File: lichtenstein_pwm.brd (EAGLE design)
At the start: 73.9 x 54.2 mm, 58 parts, among them IC1 LM2852Y-3V3, IC2 MCP23017, J1 MAGJACK, U1 ONION-OMEGA2

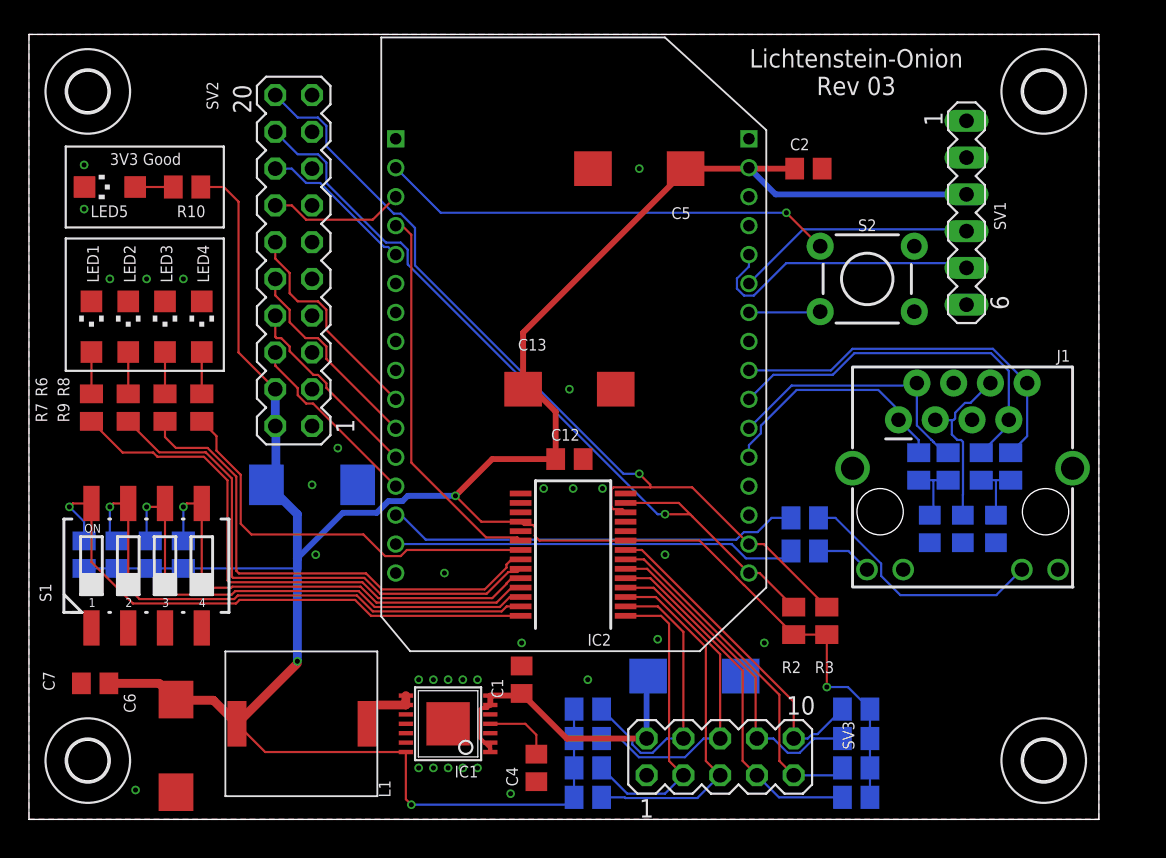
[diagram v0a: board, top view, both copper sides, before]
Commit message: Fixed some broken outputs; pwm output board added
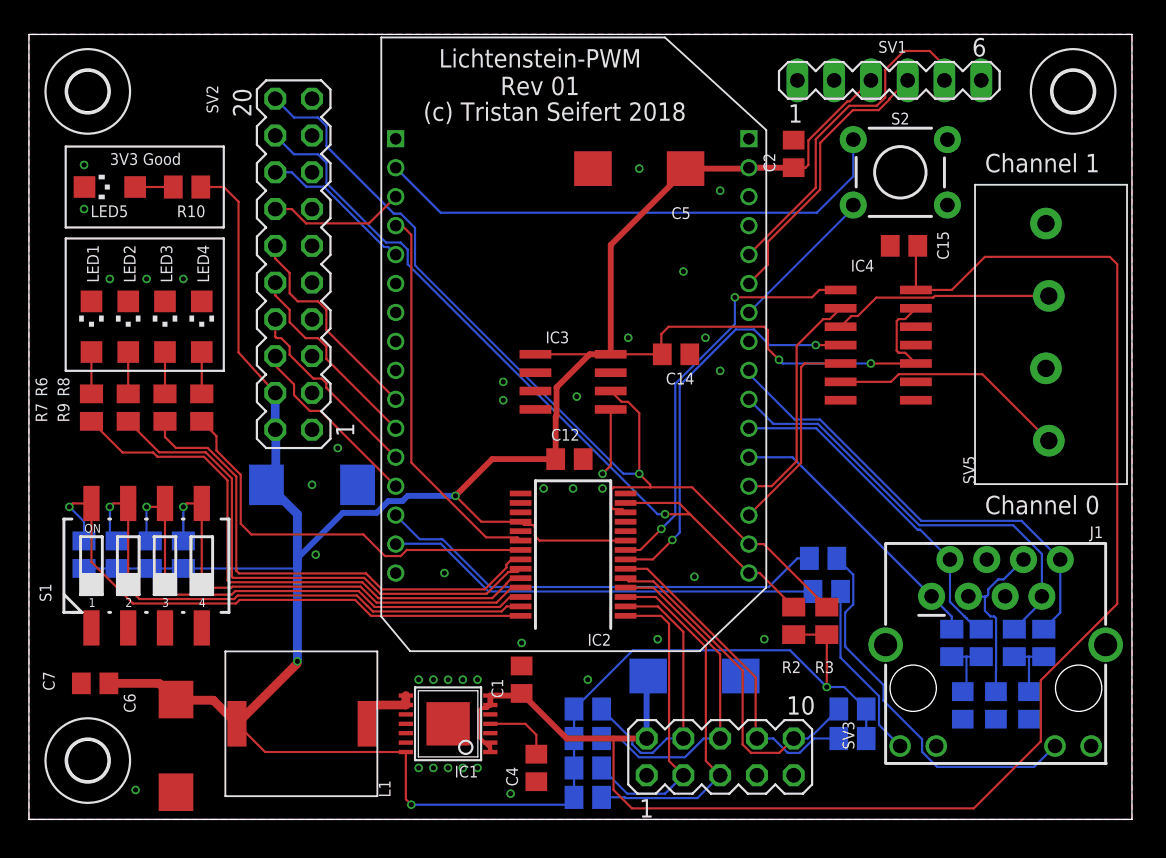
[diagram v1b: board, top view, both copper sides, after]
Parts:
- removed C13: 47µF, rcl:CT7343
- removed H2: MOUNT-HOLE2.8, holes:2,8
- removed R22, R23: 10k, rcl:M0805
- added C14, C15: 100nF, rcl:C0805
- added IC3: (no value), lichtenstein_onion:SOIC8
- added IC4: 74AHCT125SOIC14, lichtenstein_onion:SO14
- added SV5: 1792889, lichtenstein_onion:1792889
- moved C10 12.4 mm to (64.5, 7.87)
- moved C11 12.4 mm to (66.8, 7.87)
- moved J1 12.4 mm to (59.2, -2.03)
- moved R1 12.4 mm to (68.1, 12.2)
- moved R11 12.4 mm to (65.8, 12.2)
- moved R4 12.4 mm to (70.1, 12.2)
- moved R5 12.4 mm to (63.8, 12.2)
- moved C8 12.4 mm to (69.1, 7.87)
- moved SV1 10.6 mm to (59.4, 51.1), turned to 0 degrees
- moved S2 7.71 mm to (60.2, 44.7)
- moved R12 3.18 mm to (55.1, 15.7)
- moved R13 3.07 mm to (54.9, 18.0)
- moved H4 2.03 mm to (72.1, 50.3)
- moved C2 1.44 mm to (52.8, 46.0), turned to 90 degrees
- moved R24 0.25 mm to (56.9, 5.59)
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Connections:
- removed net INPUT6: IC2.5, R23.1, SV3.7
- removed net INPUT7: IC2.7, R22.1, SV3.9
- new net !PWM0_OE: IC2.8, IC4.1
- new net !PWM1_OE: IC2.7, IC4.4
- new net PWM0: IC4.2, U1.J1-13
- new net PWM1: IC4.5, U1.J1-14
- new net PWMOUT0: IC4.6, SV5.1
- new net PWMOUT1: IC4.3, SV5.3
- net +3V3: now also C14.2, IC3.1, IC3.8, IC4.10, IC4.13; no longer C13.+, R22.2, R23.2
- net GND: now also C14.1, C15.1, IC3.2, IC3.3, IC3.4, IC4.12, IC4.7, IC4.9, SV5.2, SV5.4; no longer C13.-
- net I2C_SCL: now also IC3.6
- net I2C_SDA: now also IC3.5
- net INPUT3: now also IC2.5; no longer IC2.8
- net V+: now also C15.2, IC4.14
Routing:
- net V+: track 22.1 -> 110.9 mm
- net +3V3: track 215.2 -> 244.0 mm, vias 4 -> 6
- net !PWM0_OE: track 0.00 -> 28.7 mm, vias 0 -> 2
- net !PWM1_OE: track 0.00 -> 27.8 mm, vias 0 -> 2
- net INPUT6: track 24.9 -> 0.00 mm
- net INPUT7: track 24.0 -> 0.00 mm
- net PWMOUT0: track 0.00 -> 16.5 mm
- net PWM0: track 0.00 -> 16.1 mm
- net PWMOUT1: track 0.00 -> 15.3 mm
- net PWM1: track 0.00 -> 14.6 mm
- net N$5: track 17.5 -> 26.5 mm
- net N$4: track 3.88 -> 12.4 mm
- net I2C_SCL: track 60.3 -> 67.0 mm
- net ETH_TX-: track 26.1 -> 32.3 mm
- net !FACTORY_RST: track 4.95 -> 10.4 mm
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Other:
- board size 73.9 x 54.2 mm -> 76.2 x 54.2 mm
- board text added: "Channel 0"
- board text added: "Channel 1"
- board text added: "Lichtenstein-PWM Rev 01"
- board text removed: "Lichtenstein-Onion Rev 03"

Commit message: Cleaned up traces slightly for PWM board
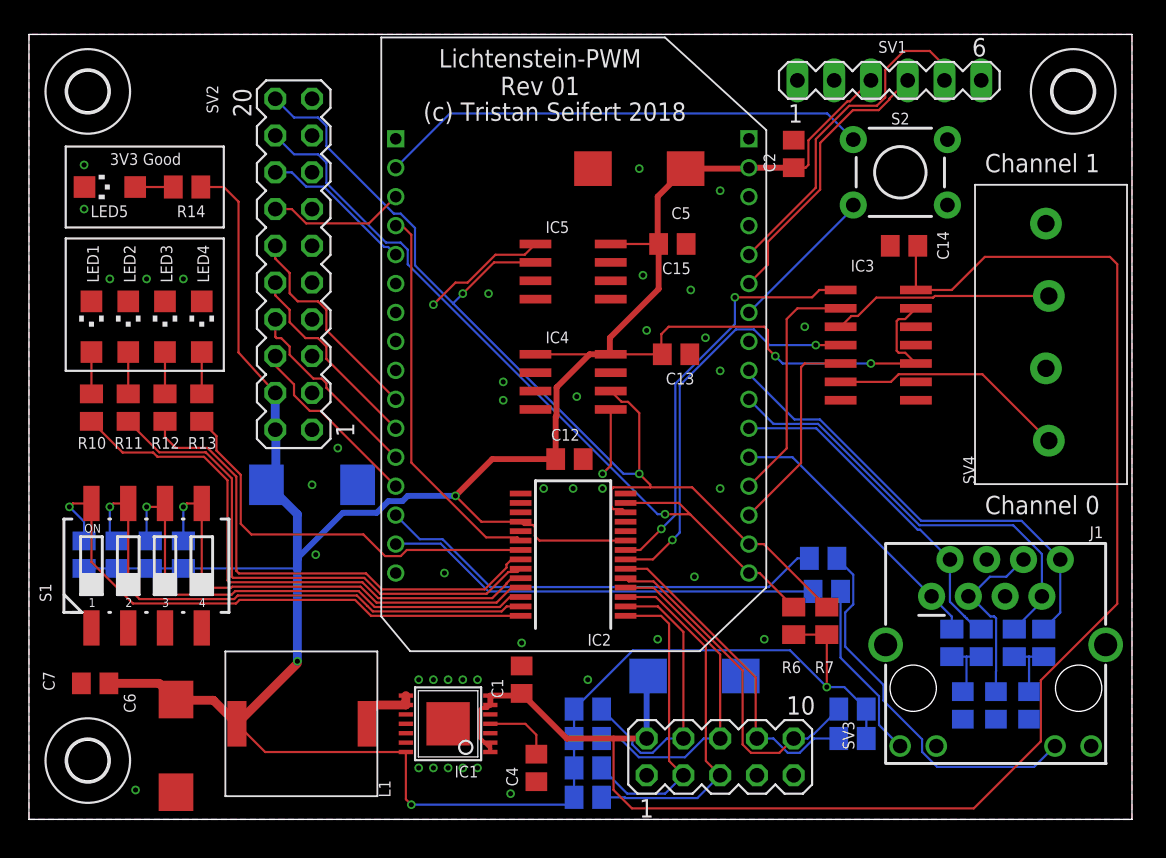
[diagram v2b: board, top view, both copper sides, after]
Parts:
- removed H4: MOUNT-HOLE2.8, holes:2,8
- removed R24, R25: 10k, rcl:M0805
- added C13: 100nF, rcl:C0805
- added H2: MOUNT-HOLE2.8, holes:2,8
- added IC5: LM75B, lichtenstein_onion:SOIC8
- added R22, R23: 680R, rcl:M0805
- IC3: value (none) -> 74AHCT125SOIC14; device lichtenstein_onion:SOIC8 -> lichtenstein_onion:SO14
- IC4: value 74AHCT125SOIC14 -> (none); device lichtenstein_onion:SO14 -> lichtenstein_onion:SOIC8
- R1, R4: value 49.9R -> 10k
- R11: value 49.9R -> 680R
- R14: value 10k -> 680R
- R15: value 10k -> 49.9R
- R2, R3: value 4k7 -> 10k
- R6, R7: value 680R -> 4k7
- R8, R9: value 680R -> 49.9R
- moved H3 68.1 mm to (72.1, 50.3)
- moved R4 66.6 mm to (3.81, 18.3), turned to 90 degrees
- moved R8 62.8 mm to (70.1, 12.2), flipped to the bottom, turned to 270 degrees
- moved R11 61.1 mm to (6.86, 28.4), flipped to the top, turned to 90 degrees
- moved R15 60.0 mm to (65.8, 12.2), turned to 270 degrees
- moved R1 57.7 mm to (10.7, 18.3), turned to 90 degrees
- moved R9 54.3 mm to (63.8, 12.2), flipped to the bottom, turned to 270 degrees
- moved R6 50.7 mm to (52.8, 13.7), turned to 270 degrees
- moved R7 50.5 mm to (55.1, 13.7), turned to 270 degrees
- moved R3 49.2 mm to (6.10, 18.3), flipped to the bottom, turned to 90 degrees
- moved R12 47.5 mm to (9.40, 28.4), flipped to the top, turned to 90 degrees
- moved R2 44.7 mm to (8.38, 18.3), flipped to the bottom, turned to 90 degrees
- moved R13 44.2 mm to (11.9, 28.4), flipped to the top, turned to 90 degrees
- moved R16 32.1 mm to (38.6, 7.62), turned to 0 degrees
- moved R17 30.7 mm to (38.6, 5.59), turned to 0 degrees
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- renumbered SV5 to SV4
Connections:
- new net !SPI_CS_1: U1.J2-6
- net !PWM0_OE: now also IC3.1; no longer IC4.1
- net !PWM1_OE: now also IC3.4; no longer IC4.4
- net +3V3: now also C13.2, C15.2, IC3.10, IC3.13, IC4.1, IC4.8, IC5.8, R1.1, R16.2, R17.2, R2.1, R3.1, R4.1, R6.2, R7.2; no longer C14.2, IC3.1, IC3.8, IC4.10, IC4.13, R10.1, R15.1, R16.1, R17.1, R2.2, R24.2, R25.2, R3.2
- net ETH_LED_ACT: now also R22.2; no longer R12.2
- net ETH_LED_LINK: now also R23.2; no longer R13.2
- net ETH_RX+: now also R9.1; no longer R5.1
- net ETH_RX-: now also R15.1; no longer R11.1
- net ETH_TX+: now also R5.1; no longer R1.1
- net ETH_TX-: now also R8.1; no longer R4.1
- net GND: now also C13.1, IC3.12, IC3.7, IC3.9, IC4.2, IC4.3, IC4.4, IC5.4, IC5.5, IC5.6, IC5.7; no longer IC3.2, IC3.3, IC3.4, IC4.12, IC4.7, IC4.9
- net I2C_SCL: now also IC4.6, IC5.2, R7.1; no longer IC3.6, R3.1
- net I2C_SDA: now also IC4.5, IC5.1, R6.1; no longer IC3.5, R2.1
- net INPUT0: now also R16.1; no longer R18.1
- net INPUT1: now also R17.1; no longer R19.1
- net INPUT2: now also R20.1; no longer R24.1
- net INPUT3: now also R21.1; no longer R25.1
- net INPUT4: now also R18.1; no longer R20.1
- net INPUT5: now also R19.1; no longer R21.1
- net N$1: now also R14.2; no longer R10.2
- net N$10: now also R12.2; no longer R8.2
- net N$11: now also R13.2; no longer R9.2
- net N$2: now also R10.2; no longer R6.2
- net N$3: now also R5.2, R8.2; no longer R1.2, R4.2
- net N$4: now also R22.1; no longer R12.1
- net N$5: now also R23.1; no longer R13.1
- net N$6: now also R15.2, R9.2; no longer R11.2, R5.2
- net N$9: now also R11.2; no longer R7.2
- net PWM0: now also IC3.2; no longer IC4.2
- net PWM1: now also IC3.5; no longer IC4.5
- net PWMOUT0: now also IC3.6; no longer IC4.6
- net PWMOUT1: now also IC3.3; no longer IC4.3
- net STATUS0: now also R10.1; no longer R6.1
- net STATUS1: now also R11.1; no longer R7.1
- net STATUS2: now also R12.1; no longer R8.1
- net STATUS3: now also R13.1; no longer R9.1
- net TEST0: now also R1.2; no longer R17.2
- net TEST1: now also R2.2; no longer R16.2
- net TEST2: now also R3.2; no longer R15.2
- net TEST3: now also R4.2; no longer R14.2
- net V+: now also C14.2, IC3.14; no longer C15.2, IC4.14
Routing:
- net I2C_SDA: track 60.9 -> 70.4 mm, vias 2 -> 3
- net I2C_SCL: track 67.0 -> 73.9 mm, vias 1 -> 2
- net +3V3: track 244.0 -> 247.4 mm
- net VDD25: track 36.5 -> 33.9 mm
- net PWM0: track 16.1 -> 16.7 mm

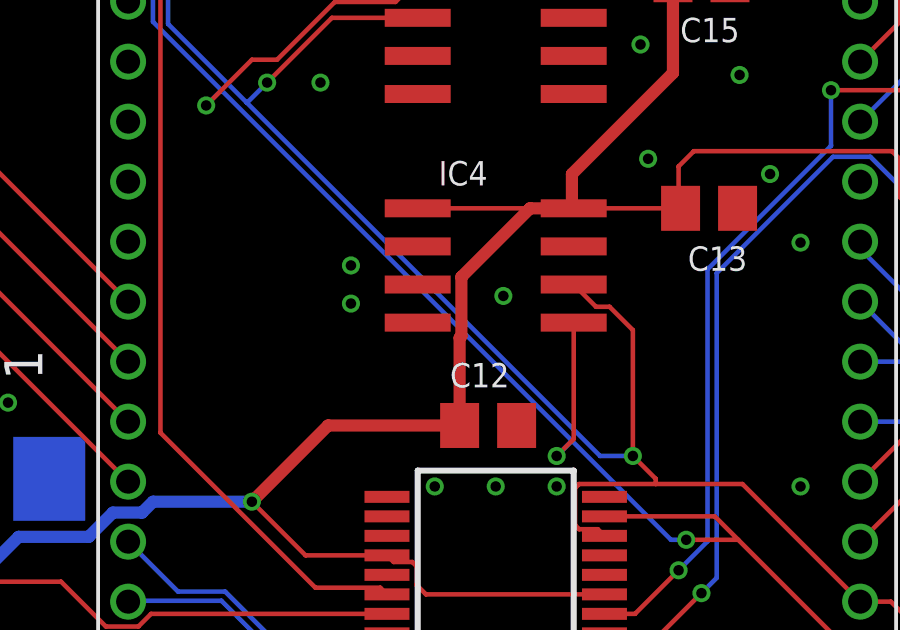
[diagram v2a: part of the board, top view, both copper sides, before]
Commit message: Added BoM for lichtenstein_pwm
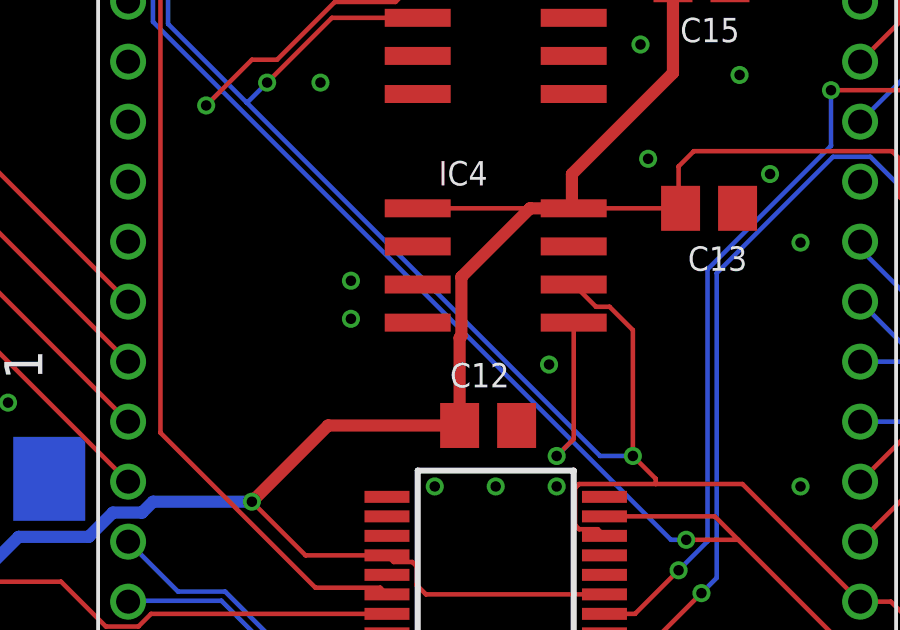
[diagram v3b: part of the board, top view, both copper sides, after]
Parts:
- moved WEED1 1.52 mm to (42.2, 27.9)
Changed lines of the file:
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@@
 <attribute name="NAME" x="65.358" y="23.162" size="0.8128" layer="25" rot="R90"/>
 </element>
-<element name="WEED1" library="lichtenstein_onion" package="DOINK" value="WEED" x="42.164" y="29.464" rot="MR0"/>
+<element name="WEED1" library="lichtenstein_onion" package="DOINK" value="WEED" x="42.164" y="27.94" rot="MR0"/>
 <element name="IC5" library="lichtenstein_onion" package="SOIC8" value="LM75B" x="37.592" y="37.846" smashed="yes" rot="R270">
 <attribute name="MOUSER" value="771-LM75BD118" x="37.592" y="37.846" size="1.778" layer="27" rot="R270" display="off"/>
@@
 <via x="3.81" y="42.164" extent="1-16" drill="0.35"/>
 <via x="42.164" y="44.958" extent="1-16" drill="0.35"/>
-<via x="37.846" y="29.21" extent="1-16" drill="0.35"/>
+<via x="39.37" y="26.924" extent="1-16" drill="0.35"/>
 <via x="37.592" y="22.86" extent="1-16" drill="0.35"/>
 <via x="35.56" y="22.86" extent="1-16" drill="0.35"/>
@@
 <via x="47.752" y="30.988" extent="1-16" drill="0.35"/>
 <via x="46.736" y="33.274" extent="1-16" drill="0.35"/>
-<via x="32.766" y="28.956" extent="1-16" drill="0.35"/>
-<via x="32.766" y="30.226" extent="1-16" drill="0.35"/>
+<via x="32.766" y="28.448" extent="1-16" drill="0.35"/>
+<via x="32.766" y="29.718" extent="1-16" drill="0.35"/>
 <contactref element="C15" pad="1"/>
 <contactref element="IC5" pad="7"/>

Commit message: updated gitignore, unpushed changes for PWM-lichtenstein board
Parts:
- moved C9 7.37 mm to (12.2, 23.1), turned to 0 degrees
- moved R23 0.25 mm to (55.1, 18.0)
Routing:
- net +3V3: track 247.4 -> 248.4 mm
